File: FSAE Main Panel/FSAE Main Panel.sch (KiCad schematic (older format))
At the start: 11 parts, among them U1 SAMD21G18A-AU, Y101 32.768kHz

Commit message: Updated PCB
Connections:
- net ~G5: now reaches U1.25
- net ~G4: now reaches U1.26
- net ~G3: now reaches U1.31
- net ~G1: now reaches U1.32
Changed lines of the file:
@@
 Wire Wire Line
 	7050 4500 7150 4500
+Text Label 7050 4000 0    50   ~ 0
+~G1
+Text Label 7450 4000 0    50   ~ 0
+~G2
+Text Label 7050 4100 0    50   ~ 0
+~G3
+Text Label 7050 4600 0    50   ~ 0
+~G4
+Text Label 7050 4700 0    50   ~ 0
+~G5
+Text Label 7200 4700 0    50   ~ 0
+~G6
 Wire Bus Line
 	7650 4100 7650 4800

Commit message: Updated PCB
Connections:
- net GEAR_IN: now also U1.19
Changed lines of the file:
@@
 Text Label 7200 4700 0    50   ~ 0
 ~G6
+Text GLabel 3750 4200 0    50   Input ~ 0
+GEAR_IN
+Wire Wire Line
+	3850 4200 3750 4200
 Wire Bus Line
 	7650 4100 7650 4800

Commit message: Updated PCB
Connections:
- net ~CHECK_ENGINE: now reaches U1.48
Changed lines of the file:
@@
 Wire Wire Line
 	3850 4200 3750 4200
+Text GLabel 7150 2100 2    39   Input ~ 0
+~CHECK_ENGINE
+Wire Wire Line
+	7150 2100 7050 2100
 Wire Bus Line
 	7650 4100 7650 4800

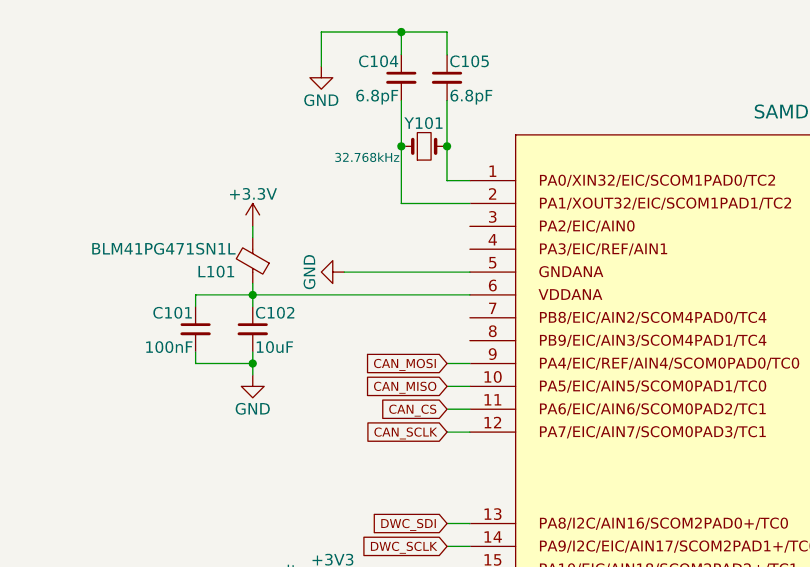
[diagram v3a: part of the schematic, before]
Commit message: Added warning nMOS circuit, simulated, updated PCB
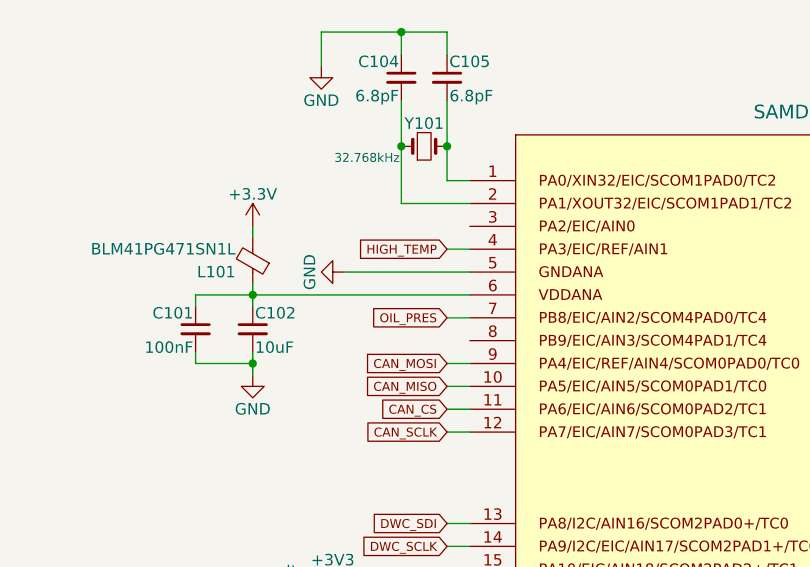
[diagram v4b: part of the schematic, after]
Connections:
- net HIGH_TEMP: now reaches U1.4
- net OIL_PRES: now reaches U1.7
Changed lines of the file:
@@
 Wire Wire Line
 	7150 2100 7050 2100
+Text GLabel 3750 2400 0    39   Input ~ 0
+HIGH_TEMP
+Text GLabel 3750 2700 0    39   Input ~ 0
+OIL_PRES
+Wire Wire Line
+	3850 2400 3750 2400
+Wire Wire Line
+	3750 2700 3850 2700
 Wire Bus Line
 	7650 4100 7650 4800

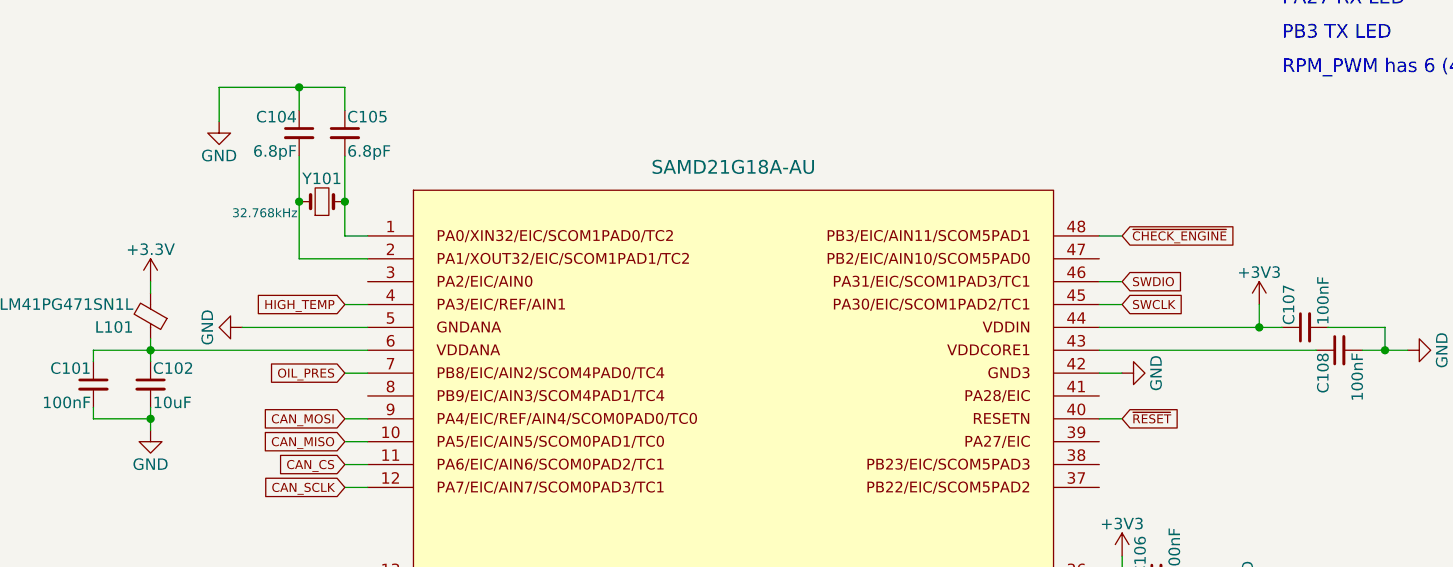
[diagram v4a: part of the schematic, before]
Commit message: Major Revision
Deleted a ton of routes, Sorry Gary.
Changed all LEDs to 1206s for better brightness
Added a lot of local net names for easier routing
Flipped J203 for better routing
Expanded board outline to fit final dashboard cutout
Added half of the Mounting Holes
Realigned RPM strip
Added Linear Reg Load Resistors to meet minimum current specs
Changed Aux load Linear Regulators to a better one
Added Separate Linear Reg for the DWC
Tuned the CAN Bus differential Pair Lines for equal length
Added decoupling capacitors at a few locations
Rerouted Power traces to be shorter and cleaner
Set up keep out zones for CAN bus interference shielding.
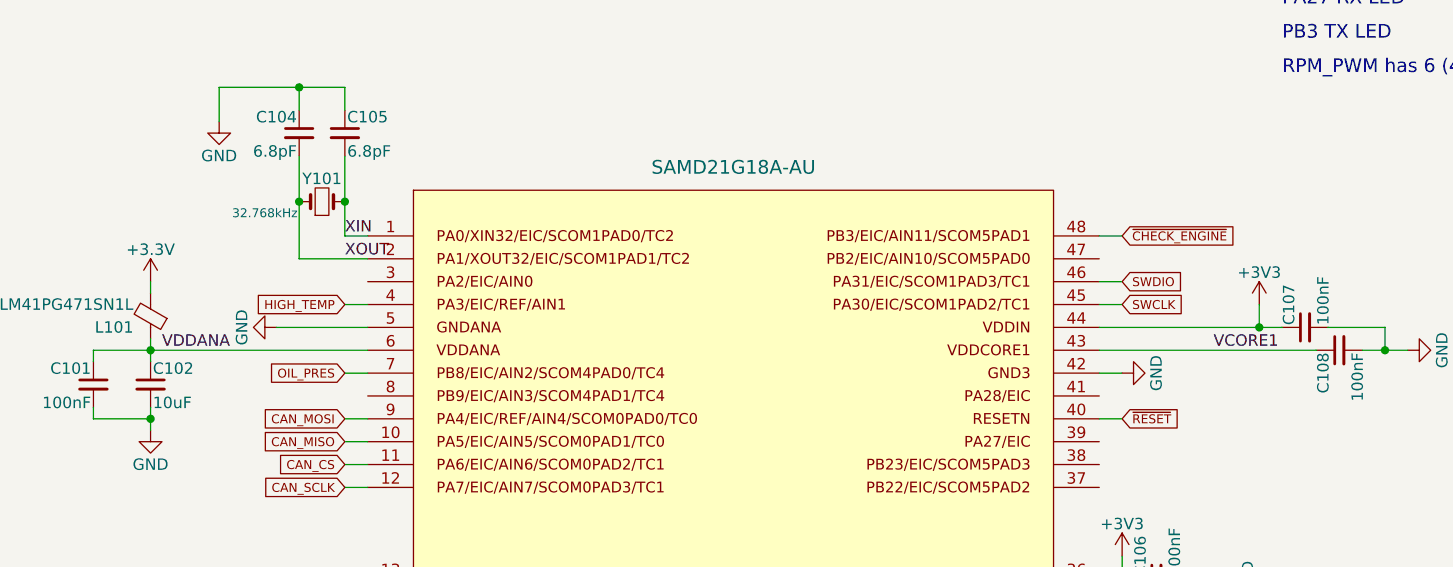
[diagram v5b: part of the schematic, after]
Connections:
- net XIN: now reaches C105.2, U1.1, Y101.2
- net XOUT: now reaches C104.2, U1.2, Y101.1
- net VCORE1: now reaches C108.1, U1.43
- net VDDANA: now reaches C101.1, C102.1, L101.1, U1.6
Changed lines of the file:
@@
 Text GLabel 3750 4600 0    39   Input ~ 0
 RPM_RCLK
-Text GLabel 9450 2100 0    39   Input ~ 0
-RPM_OUT
 Text GLabel 7150 4400 2    39   Input ~ 0
 ~GEAR_PWM
@@
 Text GLabel 7150 4200 2    39   Input ~ 0
 GEAR_SCLK
-Text GLabel 9950 2100 2    39   Input ~ 0
-GEAR_IN
 Text GLabel 7750 4800 2    39   Input ~ 0
 RPM_PWM
@@
 L power:GND #PWR0106
 U 1 1 5BF9A928
-P 3300 2500
-F 0 "#PWR0106" H 3300 2250 50  0001 C CNN
-F 1 "GND" H 3300 2350 50  0000 C CNN
-F 2 "" H 3300 2500 50  0001 C CNN
-F 3 "" H 3300 2500 50  0001 C CNN
-	1    3300 2500
+P 3450 2500
+F 0 "#PWR0106" H 3450 2250 50  0001 C CNN
+F 1 "GND" H 3450 2350 50  0000 C CNN
+F 2 "" H 3450 2500 50  0001 C CNN
+F 3 "" H 3450 2500 50  0001 C CNN
+	1    3450 2500
 	0    1    1    0
 $EndComp
@@
 	7150 3900 7050 3900
 Wire Wire Line
-	3850 2500 3300 2500
+	3850 2500 3450 2500
 Wire Wire Line
 	2900 2300 2900 2350
@@
 Wire Wire Line
 	7050 2400 7150 2400
-Wire Wire Line
-	9950 2100 9450 2100
 Wire Wire Line
 	7050 4000 7550 4000
@@
 Wire Wire Line
 	3750 2700 3850 2700
+Wire Wire Line
+	9950 2100 9450 2100
+Text GLabel 9950 2100 2    39   Input ~ 0
+GEAR_IN
+Text GLabel 9450 2100 0    39   Input ~ 0
+RPM_OUT
+Text Label 2950 2600 0    50   ~ 0
+VDDANA
+Text Label 3750 2100 0    50   ~ 0
+XIN
+Text Label 3750 2200 0    50   ~ 0
+XOUT
+Text Label 7550 2600 0    50   ~ 0
+VCORE1
 Wire Bus Line
 	7650 4100 7650 4800

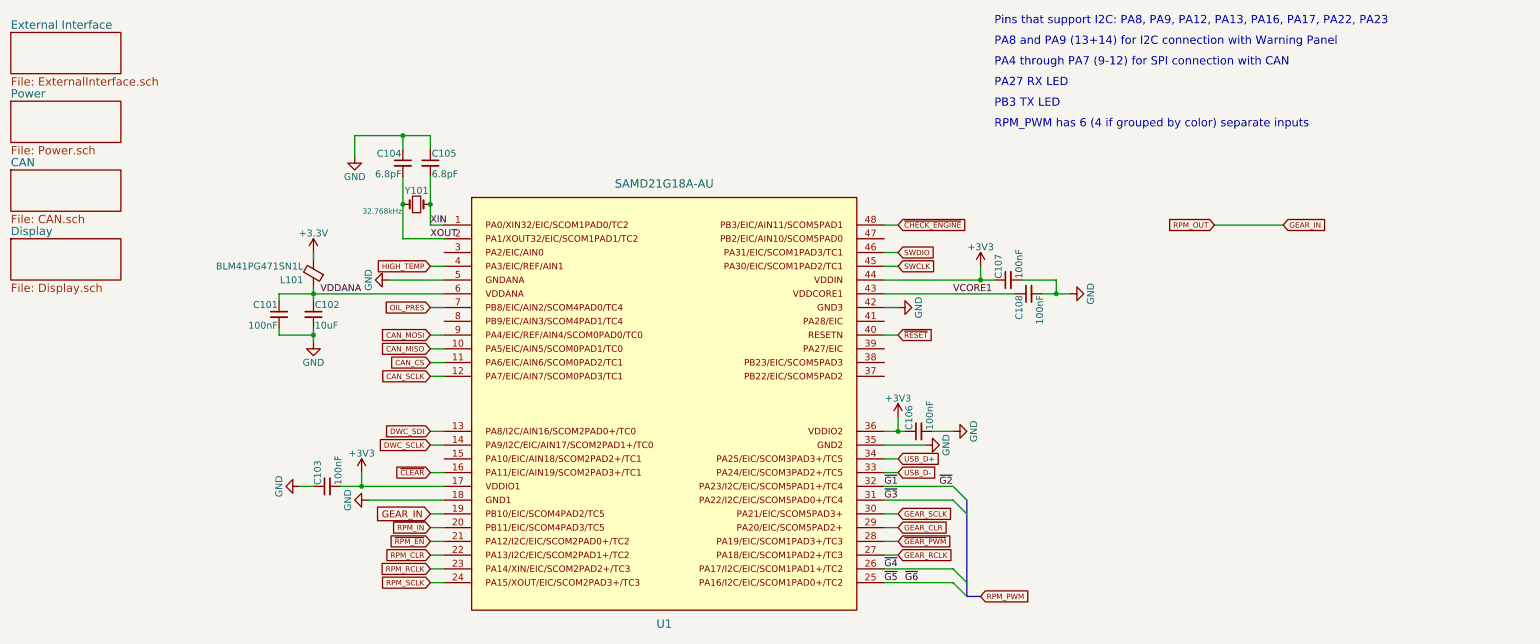
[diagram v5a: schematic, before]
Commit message: Power Supply Changes Again
Shrunk some 5V layout by switching LM7805's for their SOT223 packages but with very careful top copper considerations for thermal management.
Shrunk the Right side by 12mm for more clearance near ignition button.
Fixed Shift Register clock signal routing.
Changed shift order to be 7 segment first for easiler routing.
Added Mounting Holes.
TODO: Figure out Top layer 7 segment placement.
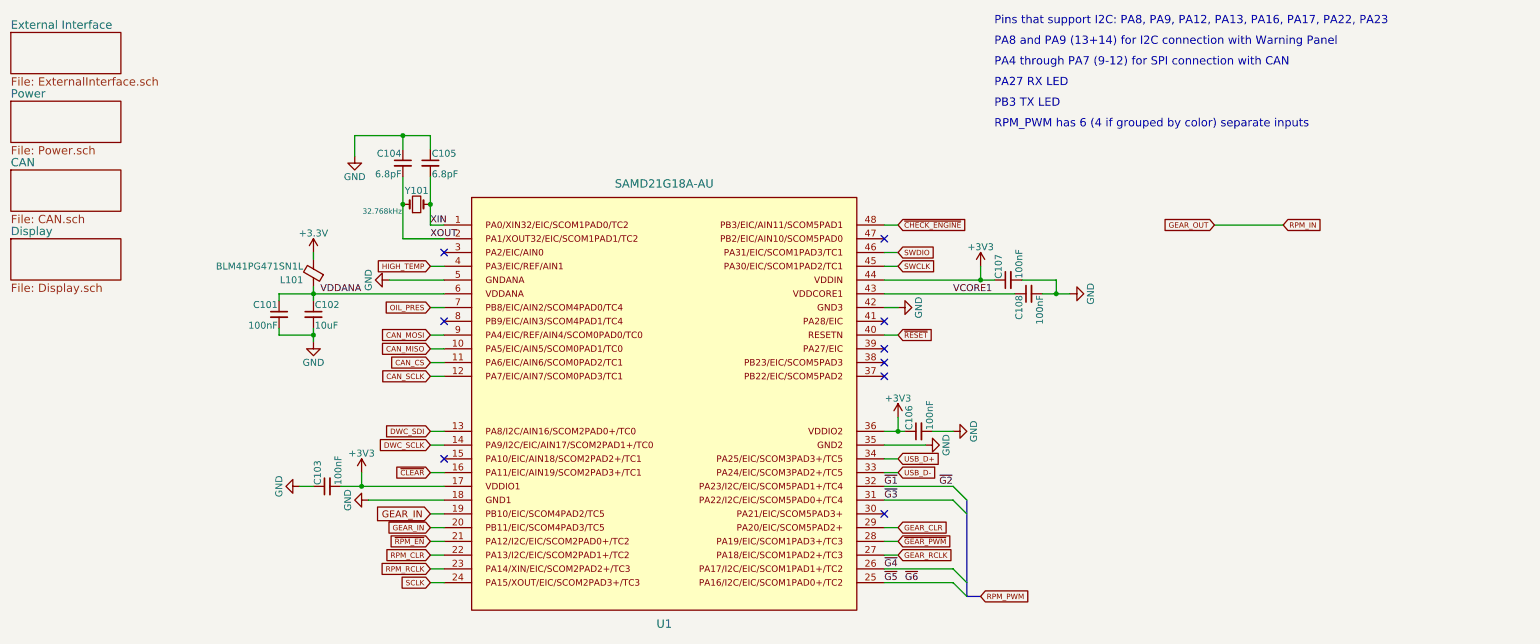
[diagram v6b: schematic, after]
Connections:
- net RPM_IN is gone; now on net GEAR_IN: U1.20
- net GEAR_SCLK: no longer names the net of U1.30
- net RPM_SCLK renamed SCLK
- no-connect marks 0 -> 9
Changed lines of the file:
@@
 Text GLabel 3750 4500 0    39   Input ~ 0
 RPM_CLR
-Text GLabel 3750 4300 0    39   Input ~ 0
+Text GLabel 9950 2100 2    39   Input ~ 0
 RPM_IN
 Text GLabel 3750 4700 0    39   Input ~ 0
-RPM_SCLK
+SCLK
 Text GLabel 3750 4600 0    39   Input ~ 0
 RPM_RCLK
@@
 Text GLabel 7150 4500 2    39   Input ~ 0
 GEAR_RCLK
-Text GLabel 7150 4200 2    39   Input ~ 0
-GEAR_SCLK
 Text GLabel 7750 4800 2    39   Input ~ 0
 RPM_PWM
@@
 	3750 2900 3850 2900
 Wire Wire Line
-	7150 4200 7050 4200
-Wire Wire Line
 	7050 4300 7150 4300
 Wire Wire Line
@@
 Wire Wire Line
 	9950 2100 9450 2100
-Text GLabel 9950 2100 2    39   Input ~ 0
+Text GLabel 3750 4300 0    39   Input ~ 0
 GEAR_IN
 Text GLabel 9450 2100 0    39   Input ~ 0
-RPM_OUT
+GEAR_OUT
 Text Label 2950 2600 0    50   ~ 0
 VDDANA
@@
 Text Label 7550 2600 0    50   ~ 0
 VCORE1
+NoConn ~ 7050 4200
+NoConn ~ 7050 3200
+NoConn ~ 7050 3100
+NoConn ~ 7050 3000
+NoConn ~ 7050 2800
+NoConn ~ 7050 2200
+NoConn ~ 3850 2300
+NoConn ~ 3850 2800
+NoConn ~ 3850 3800
 Wire Bus Line
 	7650 4100 7650 4800

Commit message: More Routing
Fixed Tactile Switch Footprints
More routing
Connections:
- net XIN renamed XIN+
- net XIN+: now also Y101.1; no longer Y101.2
- net XOUT renamed XIN-
- net XIN-: now also Y101.2; no longer Y101.1
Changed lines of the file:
@@
 P 3650 1950
 F 0 "Y101" H 3650 2050 50  0000 C CNN
-F 1 "32.768kHz" H 3400 1900 39  0000 C CNN
+F 1 "32.768kHz" H 3950 1900 39  0000 C CNN
 F 2 "MS1V-T1K:MS1V-T1K" H 3650 1950 50  0001 C CNN
 F 3 "" H 3650 1950 50  0001 C CNN
 	1    3650 1950
-	1    0    0    -1
+	-1   0    0    -1
 $EndComp
 $Comp
@@
 VDDANA
 Text Label 3750 2100 0    50   ~ 0
-XIN
+XIN+
 Text Label 3750 2200 0    50   ~ 0
-XOUT
+XIN-
 Text Label 7550 2600 0    50   ~ 0
 VCORE1

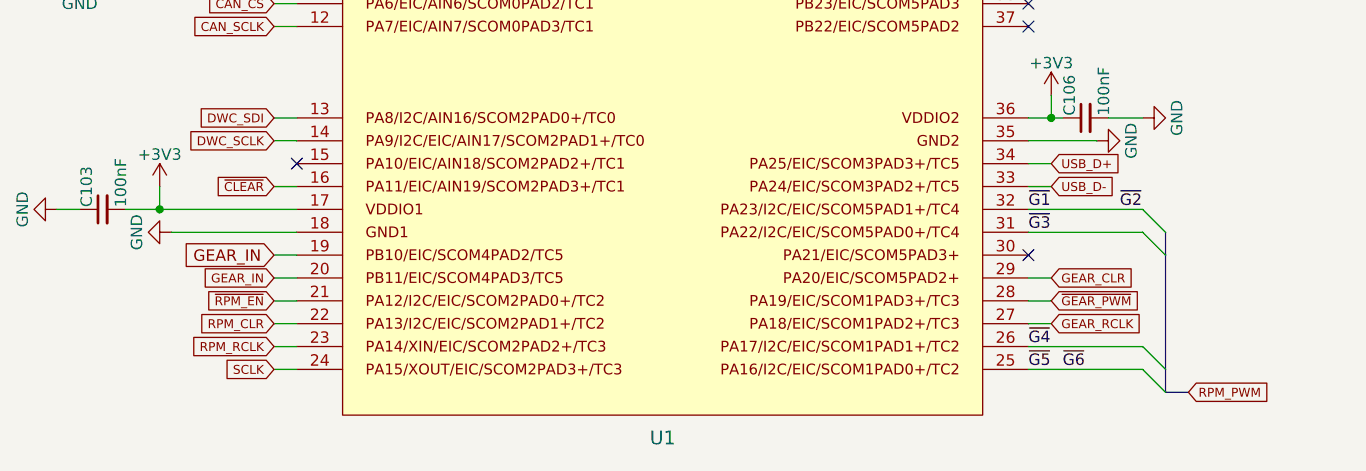
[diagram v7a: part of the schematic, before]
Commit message: Most Signal Routing
Todo: Figure out 7 segment LED placements and route their power traces
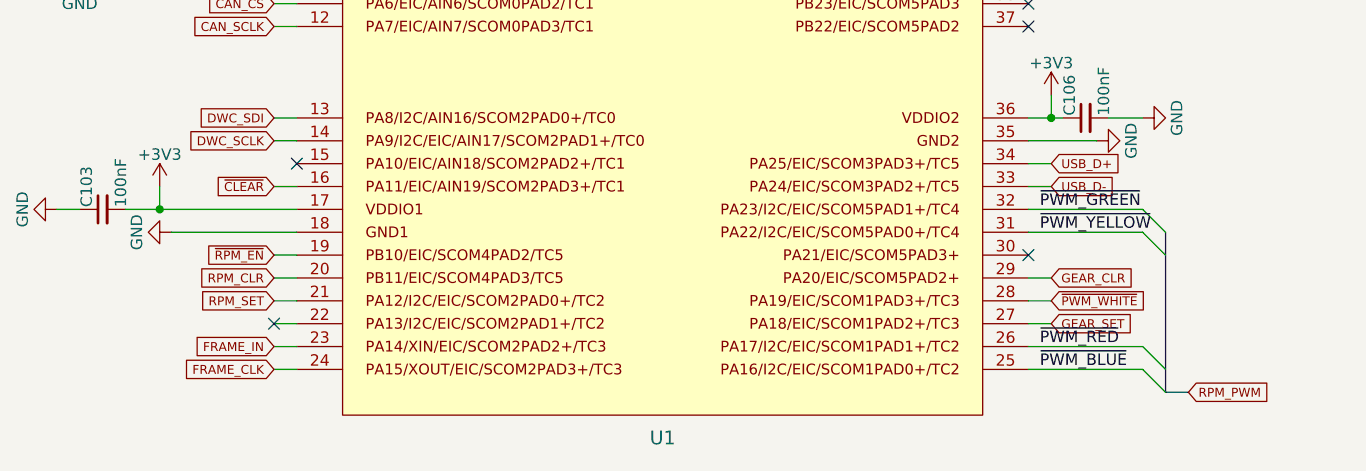
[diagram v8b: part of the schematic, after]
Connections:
- net RPM_CLR: now also U1.20; no longer U1.22
- net ~RPM_EN: now also U1.19; no longer U1.21
- removed net GEAR_IN: U1.19, U1.20
- net GEAR_RCLK renamed GEAR_SET
- net RPM_RCLK renamed FRAME_IN
- net SCLK renamed FRAME_CLK
- net ~G1 renamed ~PWM_GREEN
- net ~G3 renamed ~PWM_YELLOW
- net ~G4 renamed ~PWM_RED
- net ~G5 renamed ~PWM_BLUE
- net ~GEAR_PWM renamed ~PWM_WHITE
- new net RPM_SET: U1.21
- no-connect marks 9 -> 10
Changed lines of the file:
@@
 Text GLabel 3750 3900 0    39   Input ~ 0
 ~CLEAR
-Text GLabel 3750 4400 0    39   Input ~ 0
+Text GLabel 3750 4200 0    39   Input ~ 0
 ~RPM_EN
-Text GLabel 3750 4500 0    39   Input ~ 0
+Text GLabel 3750 4300 0    39   Input ~ 0
 RPM_CLR
 Text GLabel 9950 2100 2    39   Input ~ 0
 RPM_IN
 Text GLabel 3750 4700 0    39   Input ~ 0
-SCLK
-Text GLabel 3750 4600 0    39   Input ~ 0
-RPM_RCLK
+FRAME_CLK
+Text GLabel 3750 4400 0    39   Input ~ 0
+RPM_SET
 Text GLabel 7150 4400 2    39   Input ~ 0
-~GEAR_PWM
+~PWM_WHITE
 Text GLabel 7150 4300 2    39   Input ~ 0
 GEAR_CLR
 Text GLabel 7150 4500 2    39   Input ~ 0
-GEAR_RCLK
+GEAR_SET
 Text GLabel 7750 4800 2    39   Input ~ 0
 RPM_PWM
@@
 Wire Wire Line
 	7050 4500 7150 4500
-Text Label 7050 4000 0    50   ~ 0
-~G1
-Text Label 7450 4000 0    50   ~ 0
-~G2
-Text Label 7050 4100 0    50   ~ 0
-~G3
-Text Label 7050 4600 0    50   ~ 0
-~G4
-Text Label 7050 4700 0    50   ~ 0
-~G5
-Text Label 7200 4700 0    50   ~ 0
-~G6
-Text GLabel 3750 4200 0    50   Input ~ 0
-GEAR_IN
+Text Label 7100 4000 0    50   ~ 0
+~PWM_GREEN
+Text Label 7100 4100 0    50   ~ 0
+~PWM_YELLOW
+Text Label 7100 4600 0    50   ~ 0
+~PWM_RED
+Text Label 7100 4700 0    50   ~ 0
+~PWM_BLUE
 Wire Wire Line
 	3850 4200 3750 4200
@@
 Wire Wire Line
 	9950 2100 9450 2100
-Text GLabel 3750 4300 0    39   Input ~ 0
-GEAR_IN
+Text GLabel 3750 4600 0    39   Input ~ 0
+FRAME_IN
 Text GLabel 9450 2100 0    39   Input ~ 0
 GEAR_OUT
@@
 NoConn ~ 3850 2800
 NoConn ~ 3850 3800
+NoConn ~ 3750 4500
 Wire Bus Line
 	7650 4100 7650 4800
